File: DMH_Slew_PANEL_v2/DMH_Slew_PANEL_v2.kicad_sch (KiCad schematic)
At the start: 24 parts, among them J0 Panel_GND_Solder_Wire_Pad

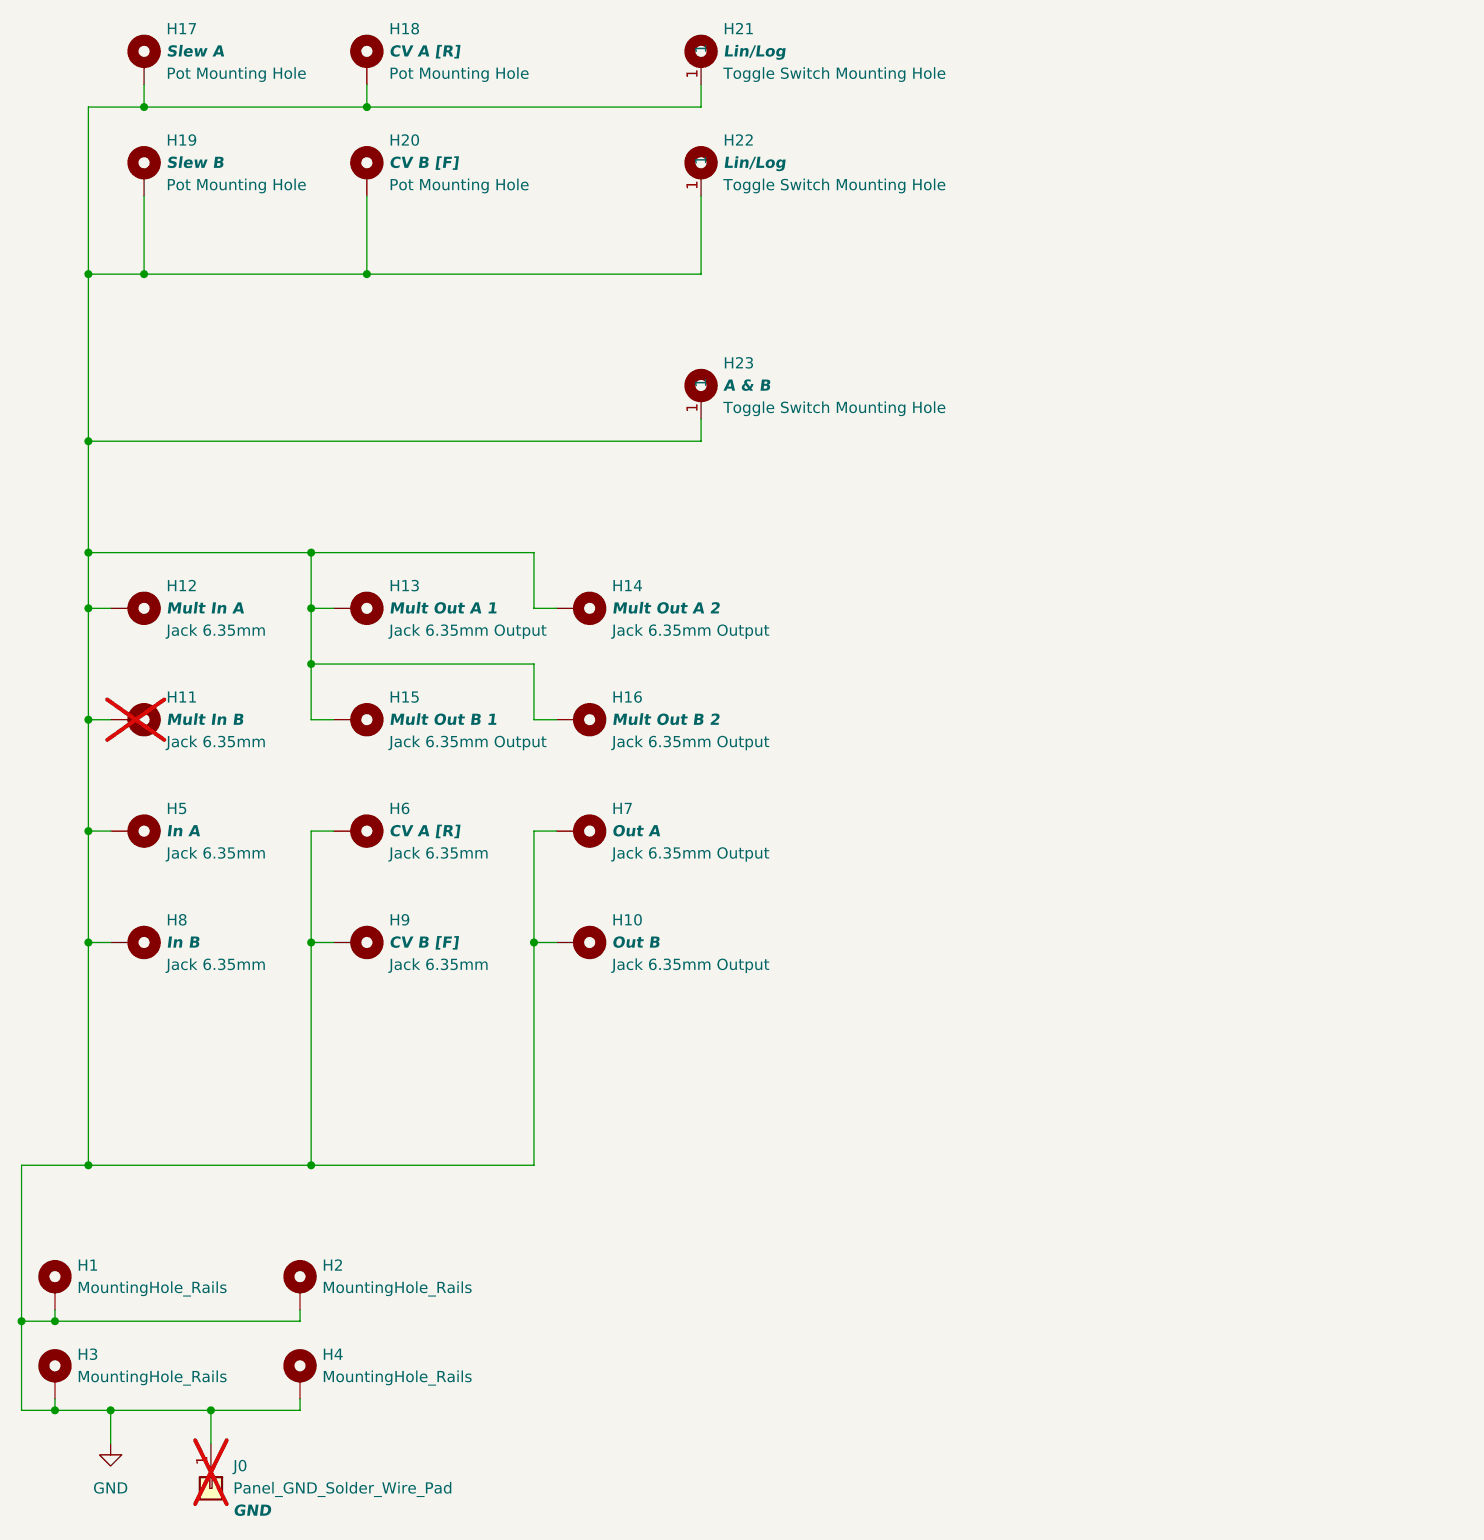
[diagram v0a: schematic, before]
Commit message: Redesigned front panel in v2
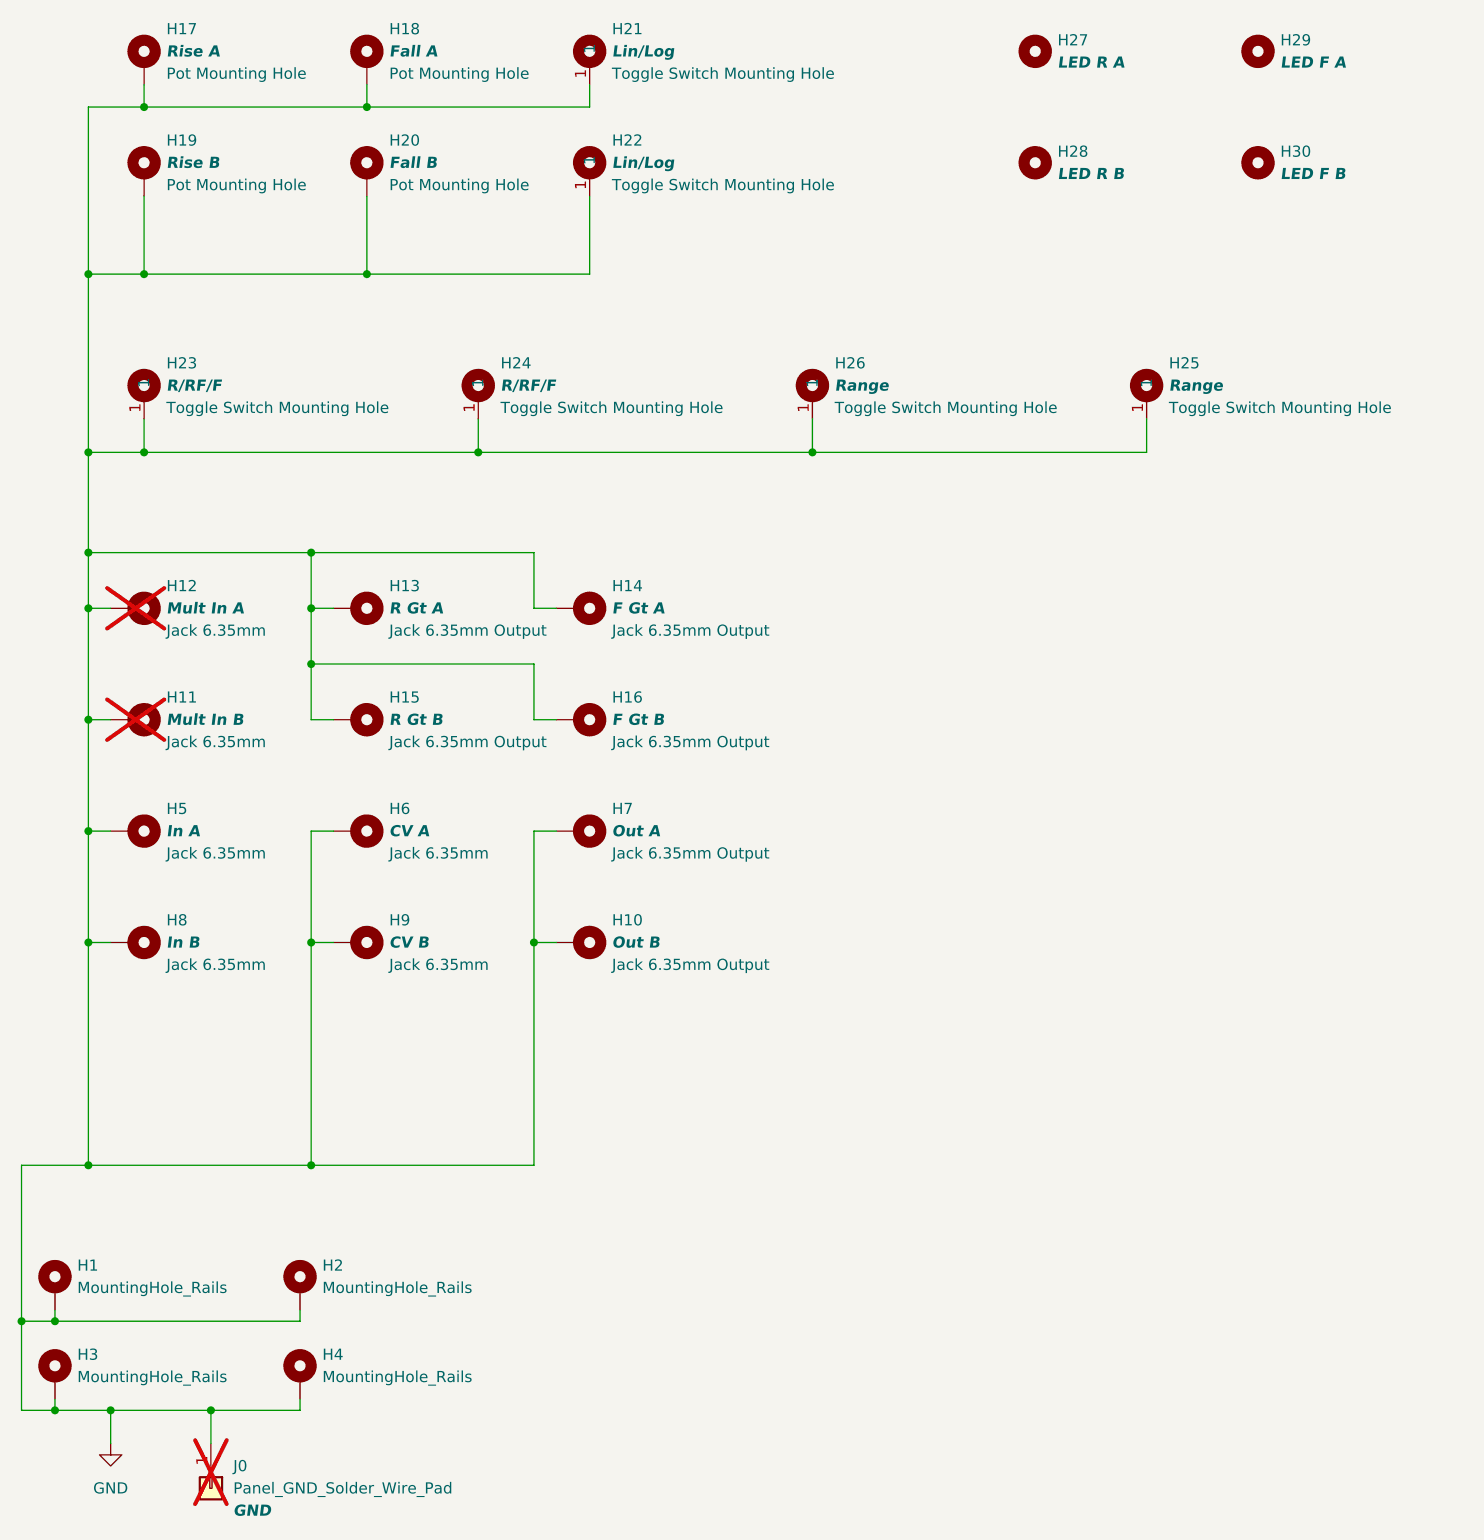
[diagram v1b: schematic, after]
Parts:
- added H24: R/RF/F, SynthStuff:Toggle_Switch_TE_Cutout, symbol SynthStuff:MountingHole_ToggleSwitch
- added H25, H26: Range, SynthStuff:Toggle_Switch_TE_Cutout, symbol SynthStuff:MountingHole_ToggleSwitch
- added H27: LED R A, SynthStuff:MountingHole_LED_3mm_R, symbol Mechanical:MountingHole
- added H28: LED R B, SynthStuff:MountingHole_LED_3mm_R, symbol Mechanical:MountingHole
- added H29: LED F A, SynthStuff:MountingHole_LED_3mm_Y, symbol Mechanical:MountingHole
- added H30: LED F B, SynthStuff:MountingHole_LED_3mm_Y, symbol Mechanical:MountingHole
- H12: now not fitted
- H13: value Mult Out A 1 -> R Gt A
- H14: value Mult Out A 2 -> F Gt A
- H15: value Mult Out B 1 -> R Gt B
- H16: value Mult Out B 2 -> F Gt B
- H17: value Slew A -> Rise A
- H18: value CV A [R] -> Fall A; footprint SynthStuff:Pot_Cutout_Tiny_attv_P110KH1 -> SynthStuff:Pot_Cutout_Small
- H19: value Slew B -> Rise B
- H20: value CV B [F] -> Fall B; footprint SynthStuff:Pot_Cutout_Tiny_attv_P110KH1 -> SynthStuff:Pot_Cutout_Small
- H23: value A & B -> R/RF/F
- H6: value CV A [R] -> CV A
- H9: value CV B [F] -> CV B
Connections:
- net GND: now also H24.1, H25.1, H26.1
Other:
- moved on the sheet: H21, H22, H23
